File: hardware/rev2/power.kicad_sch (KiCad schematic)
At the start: 20 parts, among them U5 MP2664GG-xxxx-P, U6 MAX17055ETB+, U7 TPS63805YFFR

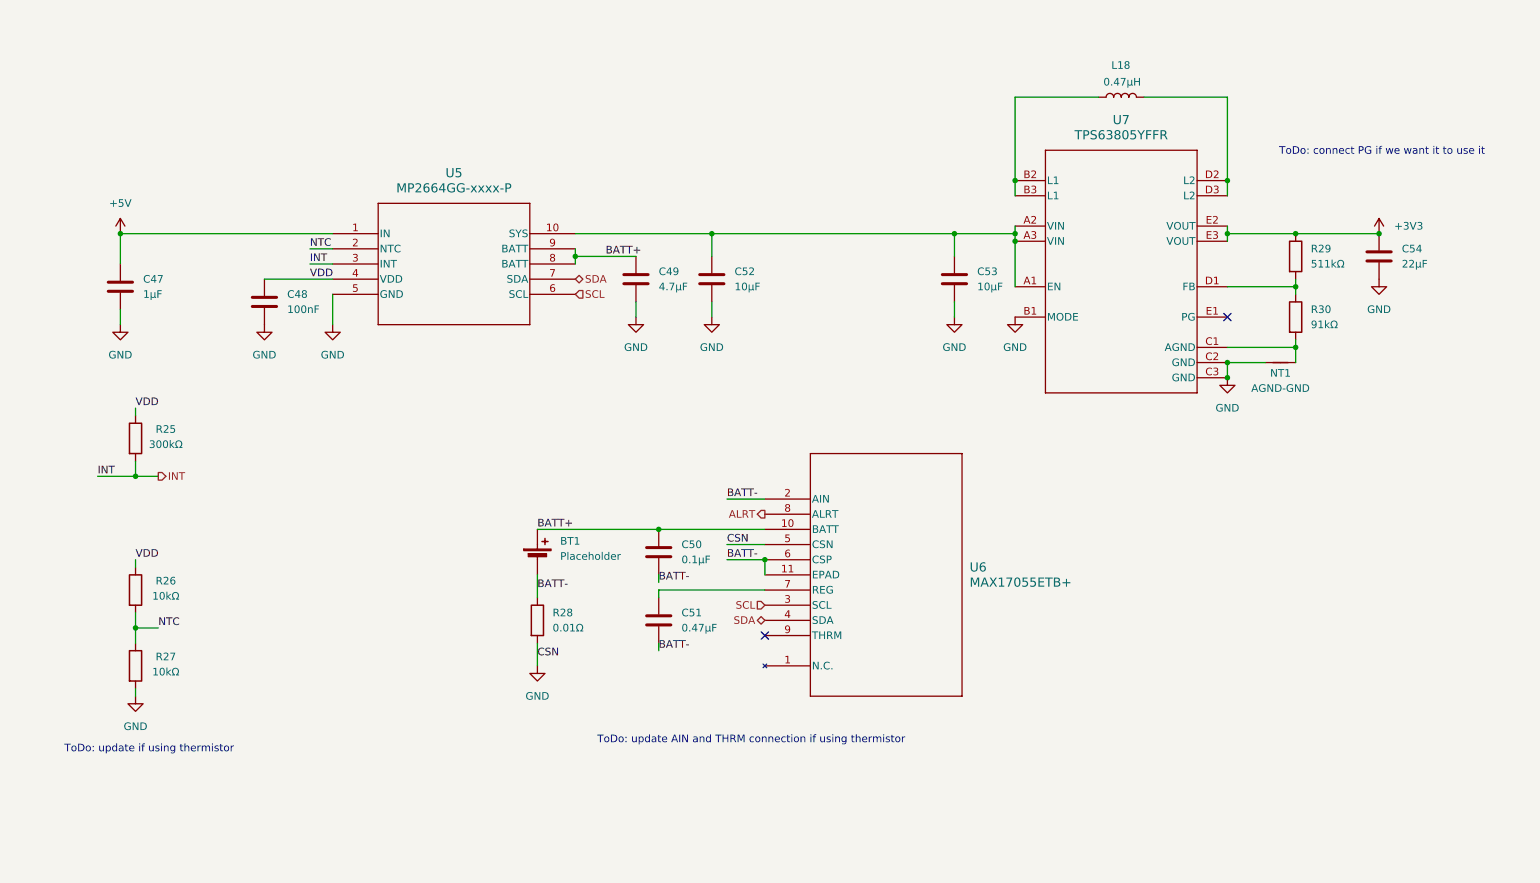
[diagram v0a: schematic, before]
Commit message: Replaced buck-boost. Added battery connector to schematic
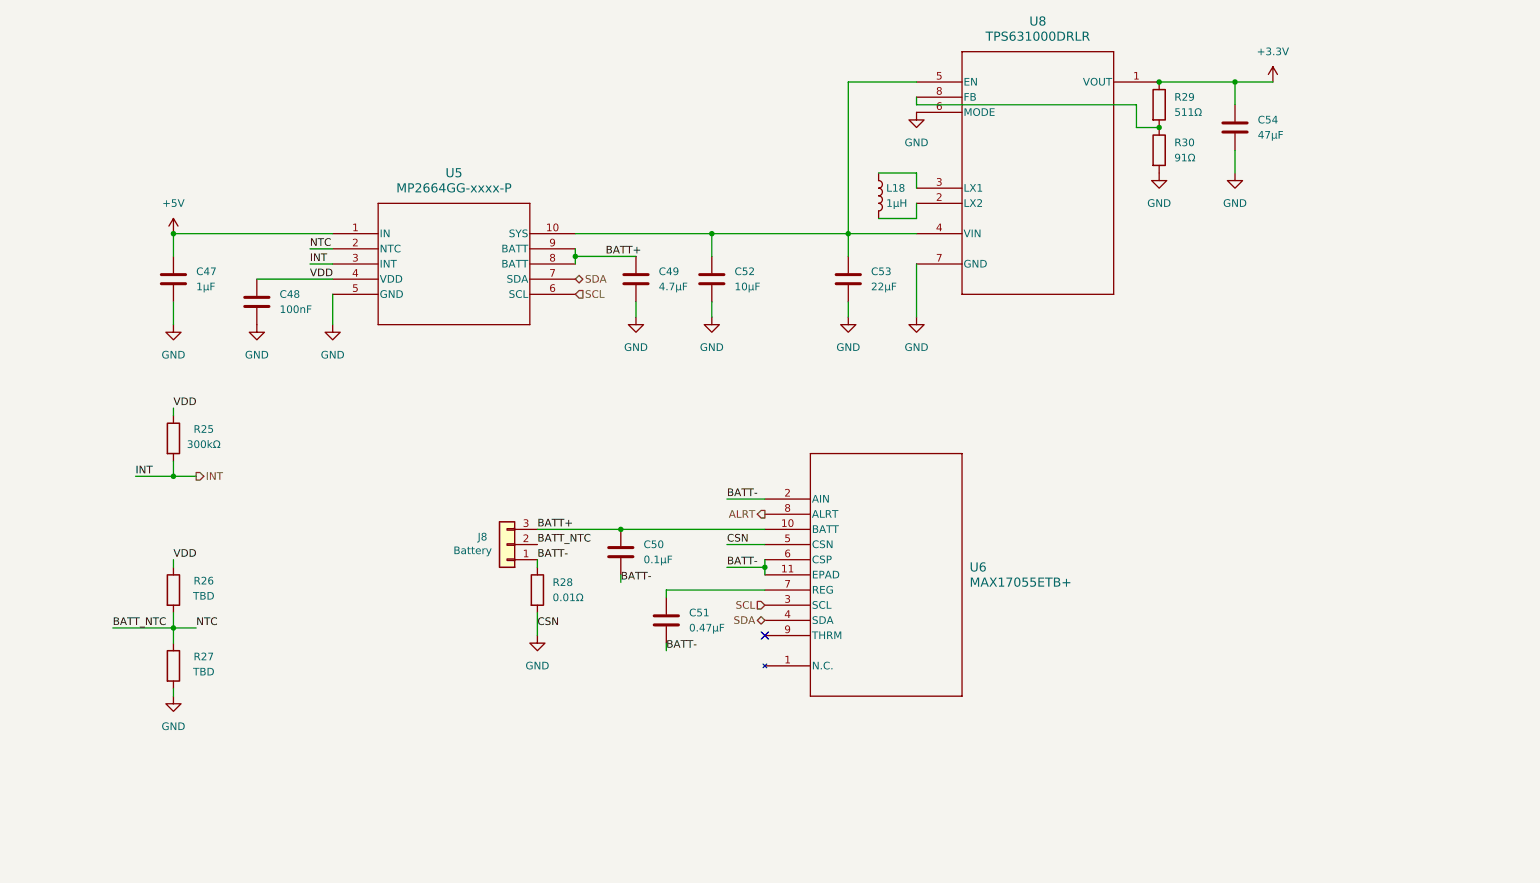
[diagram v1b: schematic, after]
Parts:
- removed BT1: Placeholder, symbol Device:Battery_Cell
- removed NT1: AGND-GND, symbol Device:NetTie_2
- removed U7: TPS63805YFFR, _footprints:YFF0015AHAN, symbol _symbols:TPS63805YFFR
- added J8: Battery, symbol Connector_Generic:Conn_01x03
- added U8: TPS631000DRLR, TPS631000DRLR_TEX, symbol _symbols:TPS631000DRLR
- C53: value 10µF -> 22µF
- C54: value 22µF -> 47µF
- L18: value 0.47µH -> 1µH
- R26, R27: value 10kΩ -> TBD
- R29: value 511kΩ -> 511Ω
- R30: value 91kΩ -> 91Ω
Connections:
- net BATT+: now also J8.3 (Pin_3)
- net BATT-: now also J8.1 (Pin_1)
- net GND: now also R30.2, U8.6 (MODE), U8.7 (GND)
- net at C52.1, C53.1, U5.10 (SYS): now also U8.4 (VIN), U8.5 (EN)
- net at R29.2, R30.1: now also U8.8 (FB)
- net at L18.1: now also U8.3 (LX1)
- net at L18.2: now also U8.2 (LX2)
- net +3V3 renamed +3.3V
- net +3.3V: now also U8.1 (VOUT)
- net NTC renamed BATT_NTC
- net BATT_NTC: now also J8.2 (Pin_2)
- no-connect marks 2 -> 1
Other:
- note removed: "ToDo: connect PG if we want it to use it"
- note removed: "ToDo: update AIN and THRM connection if using thermistor"
- note removed: "ToDo: update if using thermistor"
- moved on the sheet: C47, C48, C50, C51, R25, R26, R27, R28

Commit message: Added footprints to power components
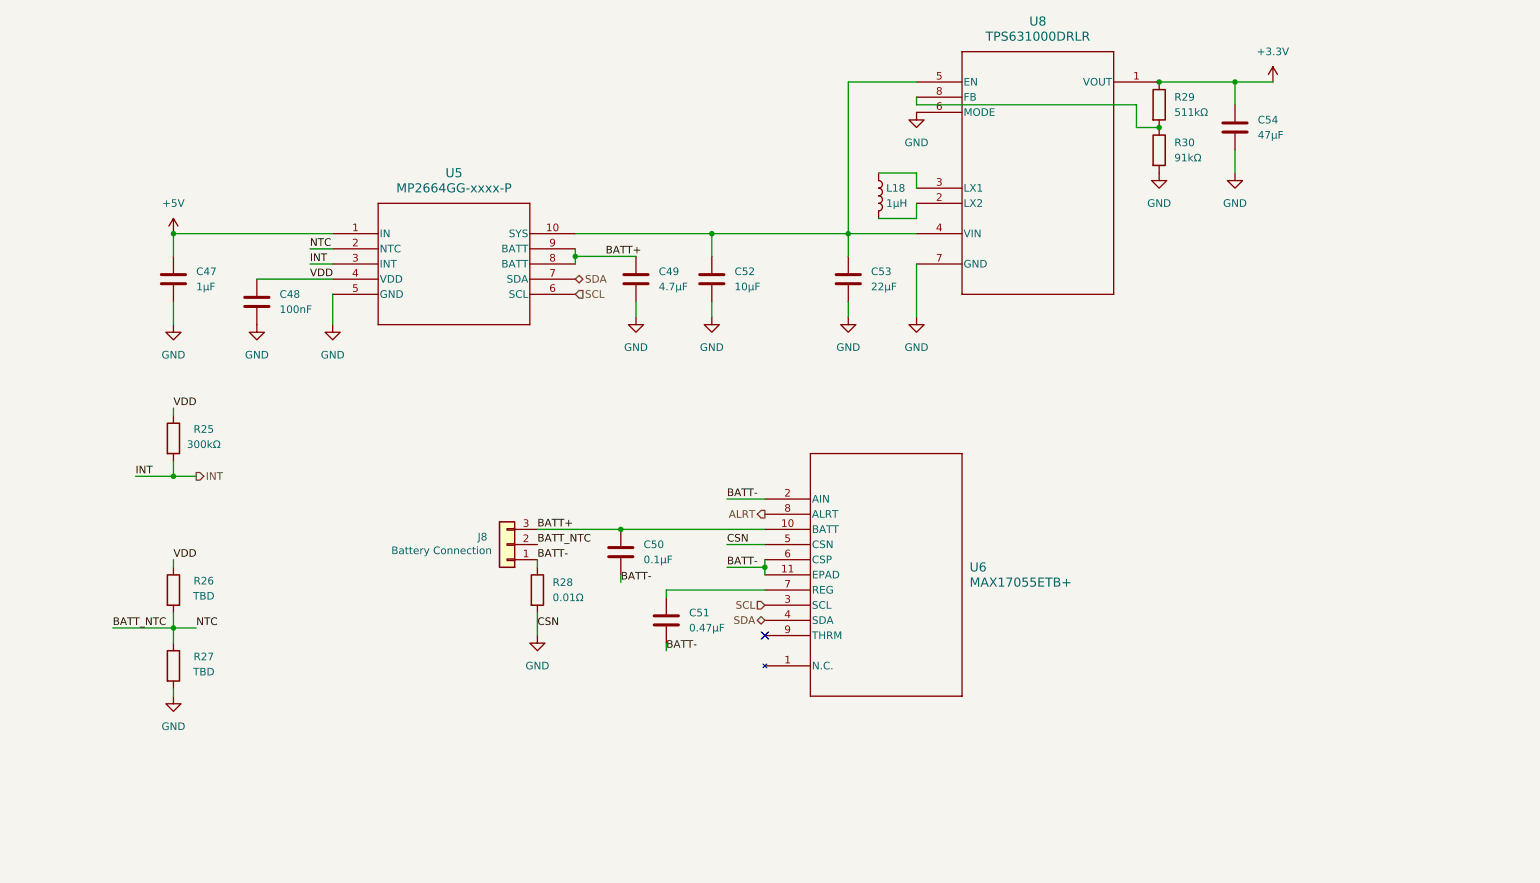
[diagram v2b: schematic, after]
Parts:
- C47, C48, C49, C50, C51, C52: footprint (none) -> Capacitor_SMD:C_0603_1608Metric_Pad1.08x0.95mm_HandSolder
- C53: footprint (none) -> Capacitor_SMD:C_0603_1608Metric_Pad1.08x0.95mm_HandSolder; Mouser Part Number (none) -> 81-GRM187R61A226ME5J
- C54: footprint (none) -> Capacitor_SMD:C_0805_2012Metric_Pad1.18x1.45mm_HandSolder; Mouser Part Number (none) -> 81-GRM219R60J476ME4D
- J8: value Battery -> Battery Connection; footprint (none) -> Connector_Molex:Molex_PicoBlade_53047-0310_1x03_P1.25mm_Vertical
- L18: footprint (none) -> _footprints:INDC2520X120N; Mouser Part Number (none) -> 81-DFE252012P-1R0MP2
- R25, R26, R27: footprint (none) -> Resistor_SMD:R_0603_1608Metric_Pad0.98x0.95mm_HandSolder
- R28: footprint (none) -> _footprints:RES_WSK2512R0100FEA; Mouser Part Number (none) -> 71-WSK2512R0100FEA
- R29: value 511Ω -> 511kΩ; footprint (none) -> Resistor_SMD:R_0603_1608Metric_Pad0.98x0.95mm_HandSolder
- R30: value 91Ω -> 91kΩ; footprint (none) -> Resistor_SMD:R_0603_1608Metric_Pad0.98x0.95mm_HandSolder
- U5: Mouser Part Number (none) -> 946-MP2664GG-0000-P
- U6: Mouser Part Number (none) -> 700-MAX17055ETB+T
- U8: Mouser Part Number (none) -> 595-TPS631000DRLR

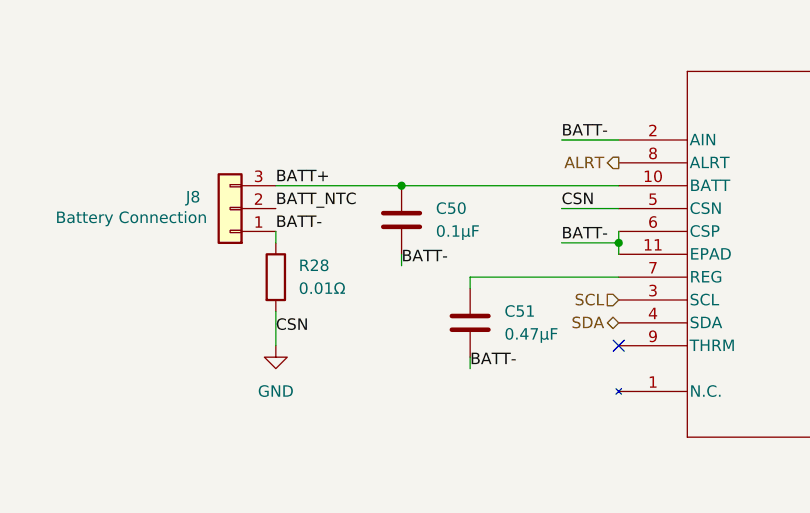
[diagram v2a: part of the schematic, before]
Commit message: Corrected sense resistor symbol
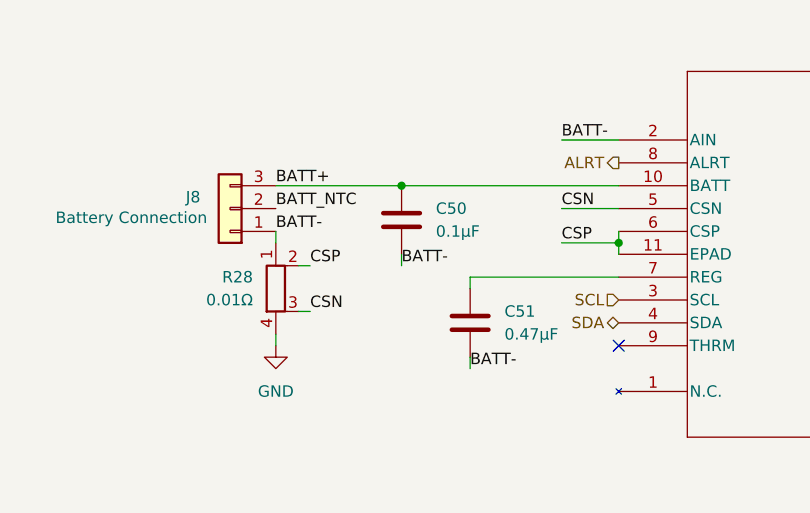
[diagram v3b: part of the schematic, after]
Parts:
- R28: symbol Device:R -> Device:R_Shunt
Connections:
- net BATT-: no longer U6.11 (EPAD), U6.6 (CSP)
- net GND: now also R28.4; no longer R28.2, U6.5 (CSN)
- new net CSN: R28.3, U6.5 (CSN)
- new net CSP: R28.2, U6.11 (EPAD), U6.6 (CSP)
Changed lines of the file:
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@@
 	(wire
 		(pts
+			(xy 101.6 138.43) (xy 102.87 138.43)
+		)
+		(stroke
+			(width 0)
+			(type default)
+		)
+	)
+	(wire
+		(pts
 			(xy 162.56 64.77) (xy 156.21 64.77)
 		)
@@
 	(wire
 		(pts
+			(xy 99.06 130.81) (xy 99.06 129.54)
+		)
+		(stroke
+			(width 0)
+			(type default)
+		)
+	)
+	(wire
+		(pts
 			(xy 128.27 74.93) (xy 105.41 74.93)
 		)
@@
 	(wire
 		(pts
+			(xy 101.6 133.35) (xy 102.87 133.35)
+		)
+		(stroke
+			(width 0)
+			(type default)
+		)
+	)
+	(wire
+		(pts
 			(xy 199.39 57.15) (xy 199.39 53.34)
 		)
@@
 	(wire
 		(pts
-			(xy 99.06 129.54) (xy 99.06 130.81)
-		)
-		(stroke
-			(width 0)
-			(type default)
-		)
-	)
-	(wire
-		(pts
 			(xy 38.1 138.43) (xy 38.1 140.97)
 		)
@@
 	(wire
 		(pts
-			(xy 162.56 88.9) (xy 162.56 80.01)
+			(xy 99.06 142.24) (xy 99.06 140.97)
 		)
 		(stroke
@@
 	(wire
 		(pts
-			(xy 120.65 135.89) (xy 120.65 134.62)
+			(xy 162.56 88.9) (xy 162.56 80.01)
 		)
 		(stroke
@@
 	(wire
 		(pts
-			(xy 99.06 138.43) (xy 99.06 142.24)
+			(xy 120.65 135.89) (xy 120.65 134.62)
 		)
 		(stroke
@@
 		)
 	)
+	(label "CSP"
+		(at 102.87 133.35 0)
+		(effects
+			(font
+				(size 1.27 1.27)
+			)
+			(justify left bottom)
+		)
+	)
 	(label "NTC"
 		(at 60.96 77.47 0)
@@
 	)
 	(label "CSN"
-		(at 99.06 140.97 0)
+		(at 102.87 138.43 0)
 		(effects
 			(font
@@
 		)
 	)
-	(label "BATT-"
+	(label "CSP"
 		(at 130.81 130.81 0)
 		(effects
@@
 	)
 	(symbol
-		(lib_id "Device:R")
-		(at 99.06 134.62 0)
+		(lib_id "Device:R_Shunt")
+		(at 99.06 135.89 0)
 		(unit 1)
 		(body_style 1)
@@
 		(fields_autoplaced yes)
 		(property "Reference" "R28"
-			(at 101.6 133.3499 0)
+			(at 96.52 134.6199 0)
 			(show_name no)
 			(do_not_autoplace no)
@@
 					(size 1.27 1.27)
 				)
-				(justify left)
+				(justify right)
 			)
 		)
 		(property "Value" "0.01Ω"
-			(at 101.6 135.8899 0)
+			(at 96.52 137.1599 0)
 			(show_name no)
 			(do_not_autoplace no)
@@
 					(size 1.27 1.27)
 				)
-				(justify left)
+				(justify right)
 			)
 		)
 		(property "Footprint" "_footprints:RES_WSK2512R0100FEA"
-			(at 97.282 134.62 90)
+			(at 97.282 135.89 90)
 			(hide yes)
 			(show_name no)
@@
 		)
 		(property "Datasheet" "https://www.vishay.com/docs/30108/wsk2512.pdf"
-			(at 99.06 134.62 0)
+			(at 99.06 135.89 0)
 			(hide yes)
 			(show_name no)
@@
 			)
 		)
-		(property "Description" "Resistor"
-			(at 99.06 134.62 0)
+		(property "Description" "Shunt resistor with Kelvin connections"
+			(at 99.06 135.89 0)
 			(hide yes)
 			(show_name no)
@@
 		)
 		(property "Sim.Type" ""
-			(at 99.06 134.62 0)
+			(at 99.06 135.89 0)
 			(hide yes)
 			(show_name no)
@@
 		)
 		(property "Mouser Part Number" "71-WSK2512R0100FEA"
-			(at 99.06 134.62 0)
+			(at 99.06 135.89 0)
 			(hide yes)
 			(show_name no)
@@
 		(pin "1"
 		)
+		(pin "3"
+		)
+		(pin "4"
+		)
 		(instances
